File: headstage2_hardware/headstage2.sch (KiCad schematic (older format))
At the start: 101 parts

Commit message: Organized changes. Converted the old kicad projects. Started 4xRHD2132 headstage version. Recompiled gtkclient_multi for Ubuntu and newer protobufs.
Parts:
- removed U?: MAX6711Z, symbol MAX6711Z
- added R32, R33, R34, R35, R36, R37, R38, R39, R40, R41, R42, R43: 0, 0402, symbol R
- added U14: MAX6711T, SC-70-4, symbol MAX6711T
- C1, C10, C11, C12, C14, C16, C17, C18, C2, C21, C24, C25, C26, C27, C28, C29, C3, C30, C31, C32, C33, C34, C35, C36, C37, C38, C39, C4, C40, C41, C42, C43, C44, C45, C5, C6, C7, C8, C9: renamed from C?; footprint (none) -> 0402
- C13, C15, C19, C20, C22, C23: renamed from C?; footprint (none) -> 0603
- D1: renamed from D?; footprint (none) -> D0603
- L1, L2: renamed from L?; footprint (none) -> 1210
- L3, L4, L5, L6: renamed from L?; footprint (none) -> 0402
- R1, R10, R11, R12, R13, R14, R15, R16, R2, R3, R4, R5, R6, R7, R8, R9: renamed from R?; footprint (none) -> 0201
- R17, R18, R19, R21, R22, R23, R24, R25, R26, R27, R28, R29, R30, R31: renamed from R?; footprint (none) -> 0402
- R20: renamed from R?; value 909K -> 909k; footprint (none) -> 0402
- U1, U2, U5, U6: renamed from U?; footprint (none) -> omnetics_36_dual
- U10: renamed from U?; footprint (none) -> QFN-10
- U11: renamed from U?; footprint (none) -> ABM10
- U12: renamed from U?; footprint (none) -> CSP_BGA-160
- U13: renamed from U?; footprint (none) -> QFN-20
- U15: renamed from U?; footprint (none) -> SOIC-8(SAE)
- U16, U18: renamed from U?; footprint (none) -> omnetics_9
- U17: renamed from U?; footprint (none) -> chip_ant
- U3, U4, U7, U8: renamed from U?; footprint (none) -> QFN-56
- U9: renamed from U?; value BatLeads -> - +; footprint (none) -> 2x100mil
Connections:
- net labels added: DR0PRI_out, DR0SEC_out, DR1PRI_out, DR1SEC_out, DROSEC_out, DT0PRI_out, DT0SEC_out, DT1PRI_out, DT1SEC_out, FSync0_out, FSync1_out, SCLK0_out, SCLK1_out
- wire segments 322 -> 325
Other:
- note added: "Reset circuit:\nAssert ~RESET\n when VDD drops below 3.08V.\nChanged from MAX6711Z, \nwhere the threshold is 2.32V for 2.8Vdd"
- note added: "Resistor ratio important,\nCheck tolerance"
- note added: "X5R or X7R dielectric;\n0402 or above\nrated >=16V"
- note removed: "Reset circuit:\nIn case of power drop"
- moved on the sheet: C11, C12, C4, C6, R18

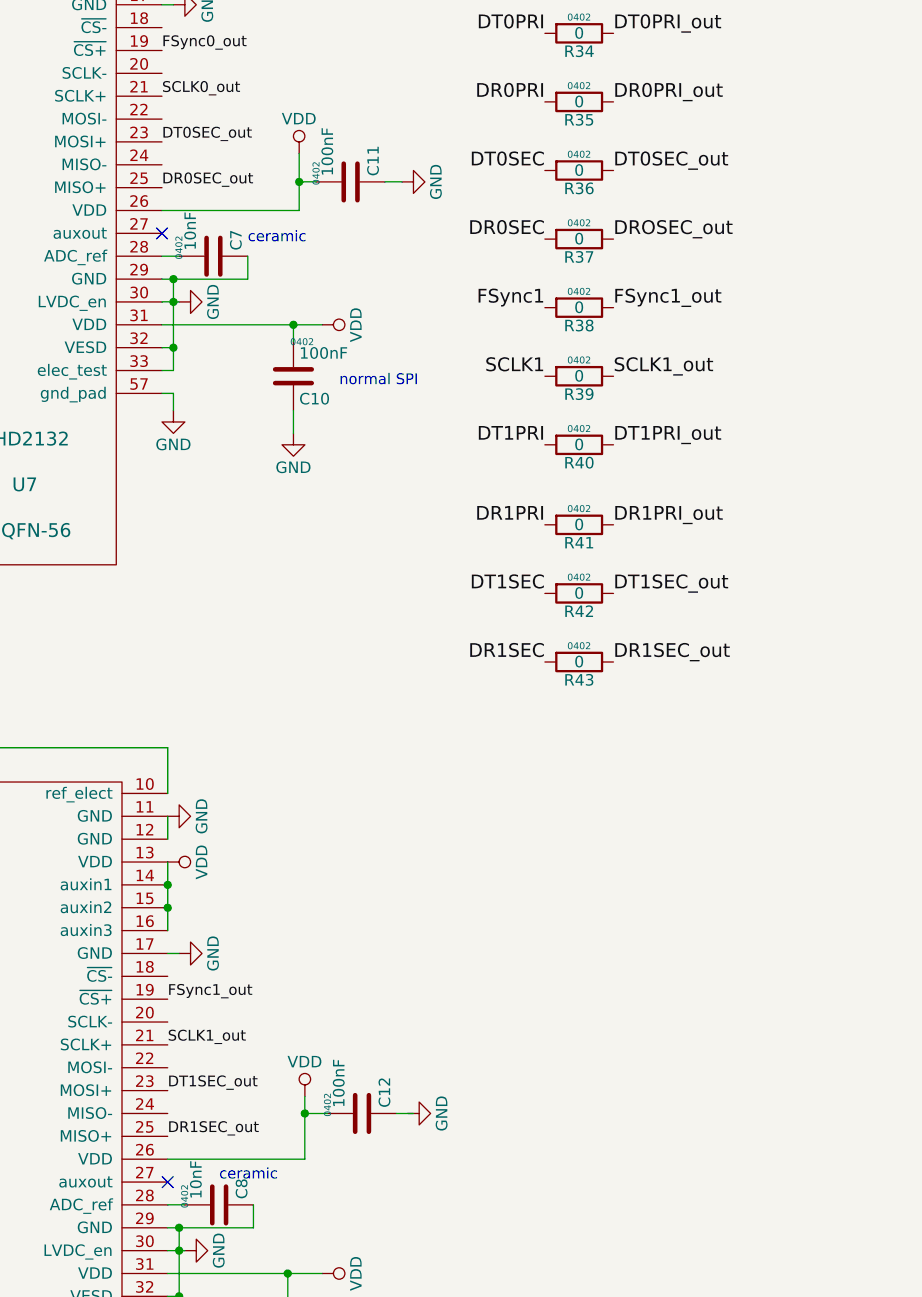
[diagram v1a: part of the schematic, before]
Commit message: Finished PCB layout, generated Gerber passed freedfm.com online check.
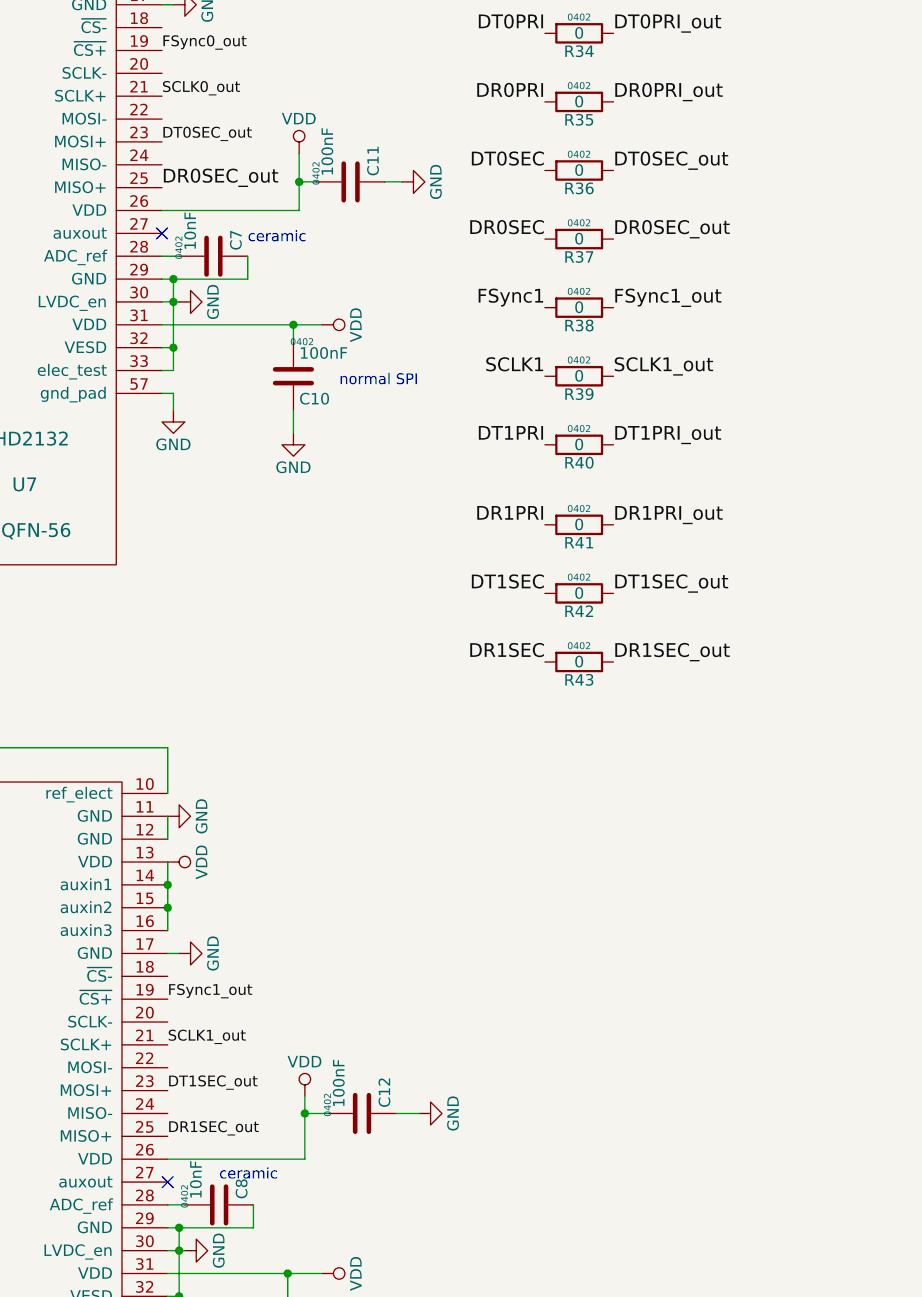
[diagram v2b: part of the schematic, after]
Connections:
- net DROSEC_out is gone; now on net DR0SEC_out: R37.1
- net GND: now also C12.1
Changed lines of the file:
@@
 L GND #PWR099
 U 1 1 557C4995
-P 12150 7075
-F 0 "#PWR099" H 12150 6825 50  0001 C CNN
-F 1 "GND" H 12150 6925 50  0000 C CNN
-F 2 "" H 12150 7075 60  0000 C CNN
-F 3 "" H 12150 7075 60  0000 C CNN
-	1    12150 7075
+P 12200 7075
+F 0 "#PWR099" H 12200 6825 50  0001 C CNN
+F 1 "GND" H 12200 6925 50  0000 C CNN
+F 2 "" H 12200 7075 60  0000 C CNN
+F 3 "" H 12200 7075 60  0000 C CNN
+	1    12200 7075
 	0    -1   -1   0
 $EndComp
@@
 Text Label 11075 2825 0    47   ~ 0
 DT0SEC_out
-Text Label 11075 3025 0    47   ~ 0
-DR0SEC_out
 Text Label 5650 6575 0    47   ~ 0
 FSync1_out
@@
 Text Label 13050 2950 0    60   ~ 0
 DT0SEC_out
-Text Label 13050 3250 0    60   ~ 0
-DROSEC_out
 Text Label 13050 3550 0    60   ~ 0
 FSync1_out
@@
 Connection ~ 11700 7075
 Wire Wire Line
-	12100 7075 12175 7075
+	12100 7075 12200 7075
 Wire Wire Line
 	11625 7900 11625 7775
@@
 Connection ~ 6225 2975
 $Comp
-L GND #PWR?
+L GND #PWR0101
 U 1 1 55989964
 P 5700 4000
-F 0 "#PWR?" H 5700 3750 50  0001 C CNN
+F 0 "#PWR0101" H 5700 3750 50  0001 C CNN
 F 1 "GND" H 5700 3850 50  0000 C CNN
 F 2 "" H 5700 4000 60  0000 C CNN
@@
 	11125 3925 11125 4000
 $Comp
-L GND #PWR?
+L GND #PWR0102
 U 1 1 5598B689
 P 11125 4000
-F 0 "#PWR?" H 11125 3750 50  0001 C CNN
+F 0 "#PWR0102" H 11125 3750 50  0001 C CNN
 F 1 "GND" H 11125 3850 50  0000 C CNN
 F 2 "" H 11125 4000 60  0000 C CNN
@@
 $EndComp
 $Comp
-L GND #PWR?
+L GND #PWR0103
 U 1 1 5598CA1A
 P 11150 8150
-F 0 "#PWR?" H 11150 7900 50  0001 C CNN
+F 0 "#PWR0103" H 11150 7900 50  0001 C CNN
 F 1 "GND" H 11150 8000 50  0000 C CNN
 F 2 "" H 11150 8150 60  0000 C CNN
@@
 	11150 8075 11150 8150
 $Comp
-L GND #PWR?
+L GND #PWR0104
 U 1 1 5598E0BB
 P 5700 8200
-F 0 "#PWR?" H 5700 7950 50  0001 C CNN
+F 0 "#PWR0104" H 5700 7950 50  0001 C CNN
 F 1 "GND" H 5700 8050 50  0000 C CNN
 F 2 "" H 5700 8200 60  0000 C CNN
@@
 Wire Wire Line
 	5700 8075 5700 8200
+Text Label 13050 3250 0    60   ~ 0
+DR0SEC_out
+Text Label 11075 3025 0    60   ~ 0
+DR0SEC_out
 $EndSCHEMATC

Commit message: Headstage2_hardware gerber gtkclient.cpp
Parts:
- C11, C12, C4, C6: Material (none) -> X5R or X7R; Tolerance (none) -> 16V
- R30: value 22K -> 200
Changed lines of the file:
@@
 F 0 "D1" H 21525 4675 50  0000 C CNN
 F 1 "LED" H 21525 4475 50  0000 C CNN
-F 2 "D0603" H 21525 4575 60  0000 C CNN
+F 2 "D0603" H 21525 4400 60  0000 C CNN
 F 3 "" H 21525 4575 60  0000 C CNN
 	1    21525 4575
@@
 P 22000 4575
 F 0 "R30" V 22080 4575 50  0000 C CNN
-F 1 "22K" V 22000 4575 50  0000 C CNN
+F 1 "200" V 22000 4575 50  0000 C CNN
 F 2 "0402" V 21930 4575 30  0000 C CNN
 F 3 "" H 22000 4575 30  0000 C CNN
@@
 	0    -1   -1   0
 $EndComp
-Text Notes 20575 5875 0    47   ~ 0
+Text Notes 20600 5825 0    47   ~ 0
 Pulled low when not used
 Text Notes 21850 5225 0    47   ~ 0
@@
 F 2 "0402" H 6513 2825 30  0000 C CNN
 F 3 "" H 6475 2975 60  0000 C CNN
+F 4 "X5R or X7R" H 6475 2975 60  0001 C CNN "Material"
+F 5 "16V" H 6475 2975 60  0001 C CNN "Tolerance"
 	1    6475 2975
 	0    1    -1   0
@@
 F 2 "0402" H 11938 2850 30  0000 C CNN
 F 3 "" H 11900 3000 60  0000 C CNN
+F 4 "X5R or X7R" H 11900 3000 60  0001 C CNN "Material"
+F 5 "16V" H 11900 3000 60  0001 C CNN "Tolerance"
 	1    11900 3000
 	0    1    -1   0
@@
 F 2 "0402" H 6488 6925 30  0000 C CNN
 F 3 "" H 6450 7075 60  0000 C CNN
+F 4 "X5R or X7R" H 6450 7075 60  0001 C CNN "Material"
+F 5 "16V" H 6450 7075 60  0001 C CNN "Tolerance"
 	1    6450 7075
 	0    1    -1   0
@@
 F 2 "0402" H 11988 6925 30  0000 C CNN
 F 3 "" H 11950 7075 60  0000 C CNN
+F 4 "X5R or X7R" H 11950 7075 60  0001 C CNN "Material"
+F 5 "16V" H 11950 7075 60  0001 C CNN "Tolerance"
 	1    11950 7075
 	0    1    -1   0
@@
 Connection ~ 8875 5475
 Wire Wire Line
-	5625 3125 6225 3125
+	6225 3125 5625 3125
 Wire Wire Line
-	6225 3125 6225 2850
+	6225 2850 6225 3125
 Wire Wire Line
 	6625 2975 6700 2975
